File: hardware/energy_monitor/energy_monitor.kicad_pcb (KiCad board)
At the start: 4 copper layers, 102.8 x 86.9 mm, 134 parts, among them J1 Screw_Terminal_01x03, J2 Screw_Terminal_01x04, J3 Screw_Terminal_01x04, J4 Screw_Terminal_01x04, J5 USB_OTG, Q1 MMBT2222, Q2 MMBT2222, U1 RAC04, U2 TPS730, U3 TPS723, U4 ADS131E08, U5 AP2112, U6 CP2104, U7 ESP-WROOM-32U

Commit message: Working on layout
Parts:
- moved C28 6.30 mm to (144.8, 59.7)
- moved C15 6.30 mm to (141.6, 56.8)
- moved C29 6.30 mm to (147.6, 57.0)
- moved U2 6.30 mm to (144.5, 57.0)
- moved C14 5.90 mm to (134.5, 66.2)
- moved C30 5.90 mm to (141.6, 65.3)
- moved C33 5.90 mm to (144.8, 67.3)
- moved C35 5.90 mm to (147.6, 64.6)
- moved U3 5.90 mm to (144.5, 64.6)
- moved U4 3.40 mm to (156.6, 80.4)
- moved C44 3.40 mm to (146.9, 78.6)
- moved C45 3.40 mm to (146.9, 80.3)
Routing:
- net /L1: track 32.9 -> 69.3 mm
- net GNDA: track 150.7 -> 171.7 mm
- added copper zone on In1.Cu, net GNDA
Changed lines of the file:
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@@
   (general
     (links 312)
-    (no_connects 240)
+    (no_connects 224)
     (area 89.924999 33.024999 192.875001 120.075001)
     (thickness 1.6)
     (drawings 14)
-    (tracks 221)
+    (tracks 228)
     (zones 0)
     (modules 134)
@@
   (layers
     (0 F.Cu signal)
-    (1 In1.Cu signal)
+    (1 In1.Cu signal hide)
     (2 In2.Cu signal)
     (31 B.Cu signal)
@@
   )
   (setup
-    (last_trace_width 0.4)
+    (last_trace_width 1)
     (user_trace_width 0.16)
     (user_trace_width 0.2)
@@
   )
   (module Capacitors_SMD:CP_Elec_6.3x5.8 (layer F.Cu)
-    (at 134.5 60.3 180)
+    (at 134.5 66.2 180)
     (descr "SMT capacitor, aluminium electrolytic, 6.3x5.8")
     (attr smd)
@@
   )
   (module Capacitors_SMD:C_0603 (layer F.Cu)
-    (at 141.6 50.5 270)
+    (at 141.6 56.8 270)
     (descr "Capacitor SMD 0603, reflow soldering, AVX (see smccp.pdf)")
     (tags "capacitor 0603")
@@
   )
   (module Capacitors_SMD:C_0603 (layer F.Cu)
-    (at 144.8 53.4 180)
+    (at 144.8 59.7 180)
     (descr "Capacitor SMD 0603, reflow soldering, AVX (see smccp.pdf)")
     (tags "capacitor 0603")
@@
   )
   (module Capacitors_SMD:C_0805 (layer F.Cu)
-    (at 147.6 50.7 270)
+    (at 147.6 57 270)
     (descr "Capacitor SMD 0805, reflow soldering, AVX (see smccp.pdf)")
     (tags "capacitor 0805")
@@
   )
   (module Capacitors_SMD:C_0603 (layer F.Cu)
-    (at 141.6 59.4 270)
+    (at 141.6 65.3 270)
     (descr "Capacitor SMD 0603, reflow soldering, AVX (see smccp.pdf)")
     (tags "capacitor 0603")
@@
   )
   (module Capacitors_SMD:C_0603 (layer F.Cu)
-    (at 144.8 61.4 180)
+    (at 144.8 67.3 180)
     (descr "Capacitor SMD 0603, reflow soldering, AVX (see smccp.pdf)")
     (tags "capacitor 0603")
@@
   )
   (module Capacitors_SMD:C_0805 (layer F.Cu)
-    (at 147.6 58.7 270)
+    (at 147.6 64.6 270)
     (descr "Capacitor SMD 0805, reflow soldering, AVX (see smccp.pdf)")
     (tags "capacitor 0805")
@@
   )
   (module Capacitors_SMD:C_0805 (layer F.Cu)
-    (at 146.9 75.2 180)
+    (at 146.9 78.6 180)
     (descr "Capacitor SMD 0805, reflow soldering, AVX (see smccp.pdf)")
     (tags "capacitor 0805")
@@
   )
   (module Capacitors_SMD:C_0603 (layer F.Cu)
-    (at 146.9 76.9)
+    (at 146.9 80.3)
     (descr "Capacitor SMD 0603, reflow soldering, AVX (see smccp.pdf)")
     (tags "capacitor 0603")
@@
   )
   (module TO_SOT_Packages_SMD:SOT-23-5 (layer F.Cu)
-    (at 144.5 50.7)
+    (at 144.5 57)
     (descr "5-pin SOT23 package")
     (tags SOT-23-5)
@@
   )
   (module TO_SOT_Packages_SMD:SOT-23-5 (layer F.Cu)
-    (at 144.5 58.7)
+    (at 144.5 64.6)
     (descr "5-pin SOT23 package")
     (tags SOT-23-5)
@@
   )
   (module Housings_QFP:TQFP-64_10x10mm_Pitch0.5mm (layer F.Cu)
-    (at 156.6 77 90)
+    (at 156.6 80.4 90)
     (descr "64-Lead Plastic Thin Quad Flatpack (PT) - 10x10x1 mm Body, 2.00 mm Footprint [TQFP] (see Microchip Packaging Specification 00000049BS.pdf)")
     (tags "QFP 0.5")
@@
   (segment (start 94.68 114.35) (end 94.68 102.695) (width 1) (layer F.Cu) (net 39))
   (segment (start 94.68 102.695) (end 94.7 102.675) (width 1) (layer F.Cu) (net 39))
+  (segment (start 94.7 79.4) (end 105.3 68.8) (width 1) (layer B.Cu) (net 40))
+  (segment (start 105.3 68.8) (end 120.6 68.8) (width 1) (layer B.Cu) (net 40))
+  (segment (start 120.6 68.8) (end 124.9 73.1) (width 1) (layer B.Cu) (net 40))
   (segment (start 105.7 77.4) (end 108.8 80.5) (width 0.4) (layer F.Cu) (net 40))
   (segment (start 108.8 80.5) (end 111.55 80.5) (width 0.4) (layer F.Cu) (net 40))
@@
   (segment (start 123.45 80.5) (end 125.05 80.5) (width 0.4) (layer F.Cu) (net 55))
   (segment (start 123.45 87) (end 125.05 87) (width 0.4) (layer F.Cu) (net 56))
+  (segment (start 102.2 81.6) (end 102.2 83.7) (width 1) (layer B.Cu) (net 97))
+  (segment (start 102.2 83.7) (end 100 85.9) (width 1) (layer B.Cu) (net 97))
+  (segment (start 99.76 114.35) (end 99.76 86.14) (width 1) (layer B.Cu) (net 97))
+  (segment (start 99.76 86.14) (end 100 85.9) (width 1) (layer B.Cu) (net 97))
+  (segment (start 117.4 73.1) (end 107.3 73.1) (width 1) (layer B.Cu) (net 97))
+  (segment (start 107.3 73.1) (end 102.2 78.2) (width 1) (layer B.Cu) (net 97))
+  (segment (start 102.2 78.2) (end 102.2 81.6) (width 1) (layer B.Cu) (net 97))
   (segment (start 127.95 83.8) (end 106.8 83.8) (width 0.4) (layer F.Cu) (net 97))
   (segment (start 106.8 83.8) (end 104.6 81.6) (width 0.4) (layer F.Cu) (net 97))
@@
   (segment (start 121.15 102.8) (end 121.15 105.25) (width 0.4) (layer F.Cu) (net 97))
   (segment (start 121.15 105.25) (end 120.6 105.8) (width 0.4) (layer F.Cu) (net 97))
-  (segment (start 102.2 81.6) (end 102.2 83.7) (width 1) (layer F.Cu) (net 97))
-  (segment (start 102.2 83.7) (end 100 85.9) (width 1) (layer F.Cu) (net 97))
-  (segment (start 99.76 114.35) (end 99.76 86.14) (width 1) (layer F.Cu) (net 97))
   (segment (start 99.76 86.14) (end 100 85.9) (width 1) (layer F.Cu) (net 97))
+  (zone (net 97) (net_name GNDA) (layer In1.Cu) (hatch edge 0.508)
+    (connect_pads (clearance 0.508))
+    (min_thickness 0.254)
+    (fill yes (arc_segments 16) (thermal_gap 0.508) (thermal_bridge_width 0.508))
+    (polygon
+      (pts
+        (xy 112 122) (xy 195 122) (xy 195 87) (xy 162 87) (xy 162 66)
+        (xy 152 66) (xy 152 46) (xy 142 46) (xy 142 31) (xy 88 31)
+        (xy 88 65) (xy 131 65) (xy 131 92) (xy 112 92)
+      )
+    )
+  )
 )

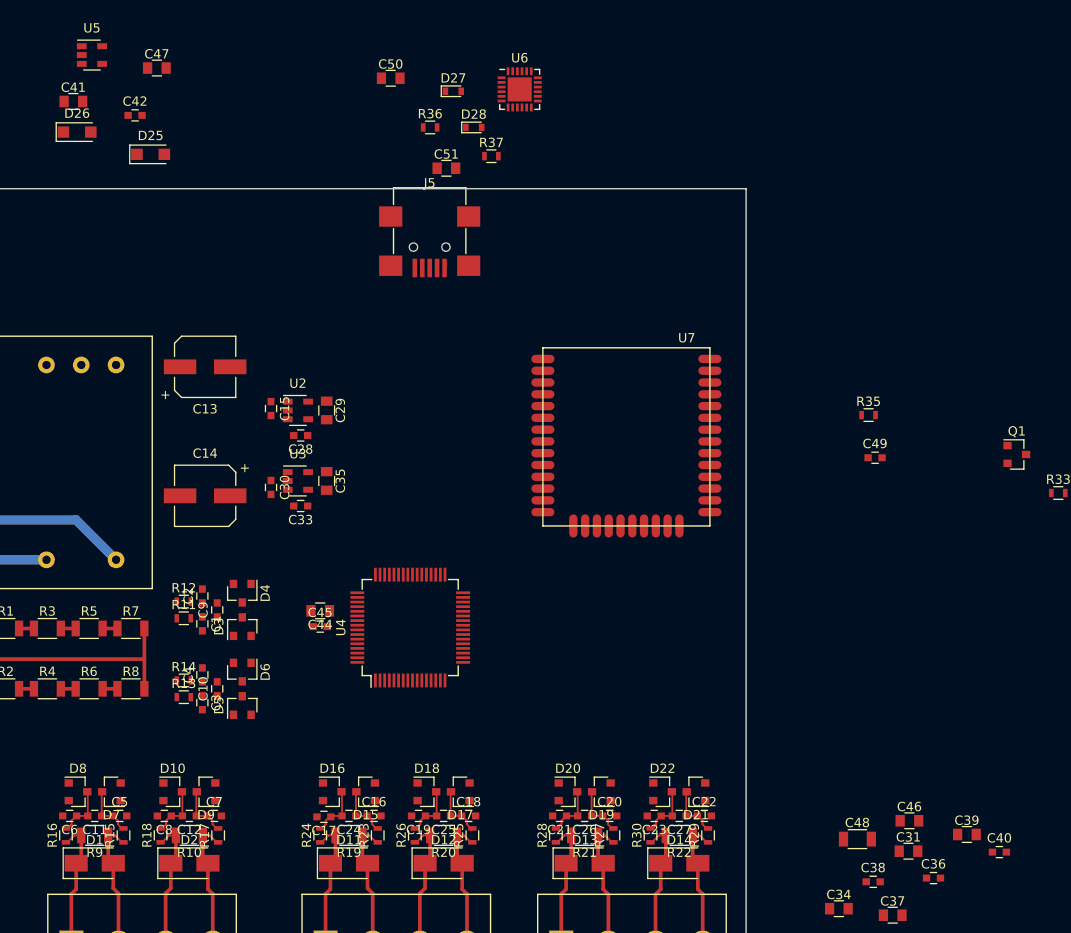
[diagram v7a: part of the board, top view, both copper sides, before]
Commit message: Added digital isolator to USB UART circuit
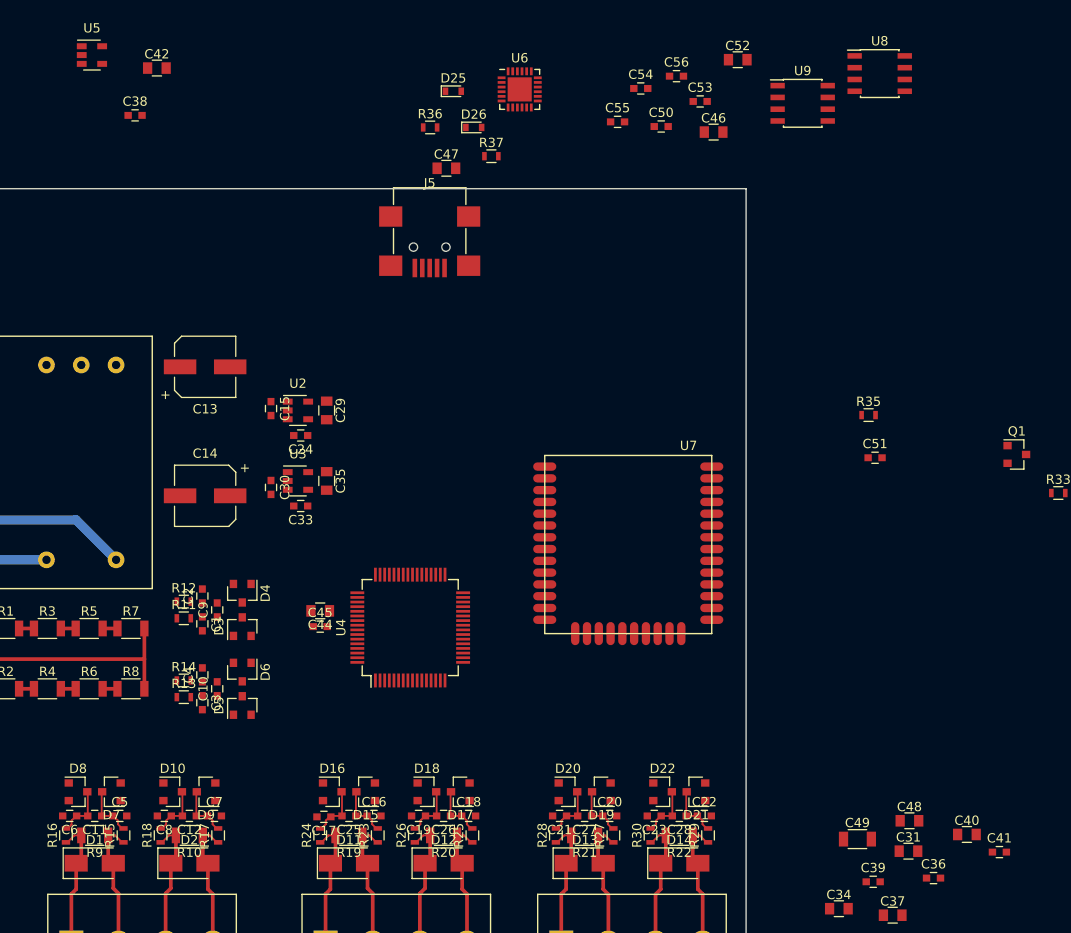
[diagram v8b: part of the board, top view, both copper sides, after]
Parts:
- removed the C41 at (120.3, 23.7)
- removed the D25 at (128.6, 29.4)
- removed the D26 at (120.7, 27.0)
- added C46: 1u, Capacitors_SMD:C_0805, F.Cu at (189.3, 27.0)
- added C52: 1u, Capacitors_SMD:C_0805, F.Cu at (191.9, 19.2)
- added C53: 0.1u, Capacitors_SMD:C_0603, F.Cu at (187.8, 23.7)
- added C54: 0.1u, Capacitors_SMD:C_0603, F.Cu at (181.4, 22.3)
- added C55: 0.1u, Capacitors_SMD:C_0603, F.Cu at (178.9, 25.9)
- added C56: 0.1u, Capacitors_SMD:C_0603, F.Cu at (185.3, 21.0)
- added U8: ISO7421, Housings_SOIC:SOIC-8_3.9x4.9mm_Pitch1.27mm, F.Cu at (207.2, 20.7)
- added U9: ISO7420, Housings_SOIC:SOIC-8_3.9x4.9mm_Pitch1.27mm, F.Cu at (198.9, 23.9)
- C50: value 10u -> 0.1u; footprint Capacitors_SMD:C_0805 -> Capacitors_SMD:C_0603
- moved C50 29.6 mm to (183.7, 26.4)
- moved U7 11.6 mm to (180.1, 68.3)
- renumbered C28 to C24, C24 to C25, C25 to C26, C26 to C27, C27 to C28, C42 to C38, C38 to C39, C39 to C40, C40 to C41, C47 to C42, C51 to C47, C46 to C48, C48 to C49, C49 to C51, D27 to D25, D28 to D26
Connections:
- C38 pad 1: Net-(C41-Pad1) -> +5V
- C47 pad 2: GNDA -> GND
- C50 pad 1: +3V3 -> VCC
- C50 pad 2: GNDA -> GND
- J5 pad 5: GNDA -> GND
- R36 pad 1: +3V3 -> VCC
- R37 pad 1: +3V3 -> VCC
- U5 pad 1: Net-(C41-Pad1) -> +5V
- U5 pad 3: Net-(C41-Pad1) -> +5V
- U6 pad 19: /RTS -> Net-(U6-Pad19)
- U6 pad 2: GNDA -> GND
- U6 pad 20: /TXD0 -> Net-(U6-Pad20)
- U6 pad 21: /RXD0 -> Net-(U6-Pad21)
- U6 pad 23: /DTR -> Net-(U6-Pad23)
- U6 pad 25: GNDA -> GND
- U6 pad 5: +3V3 -> VCC
- U6 pad 6: +3V3 -> VCC
- U6 pad 7: +3V3 -> /VUSB
